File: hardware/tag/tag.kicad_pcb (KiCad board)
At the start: 2 copper layers, 96.5 x 48.3 mm, 14 parts

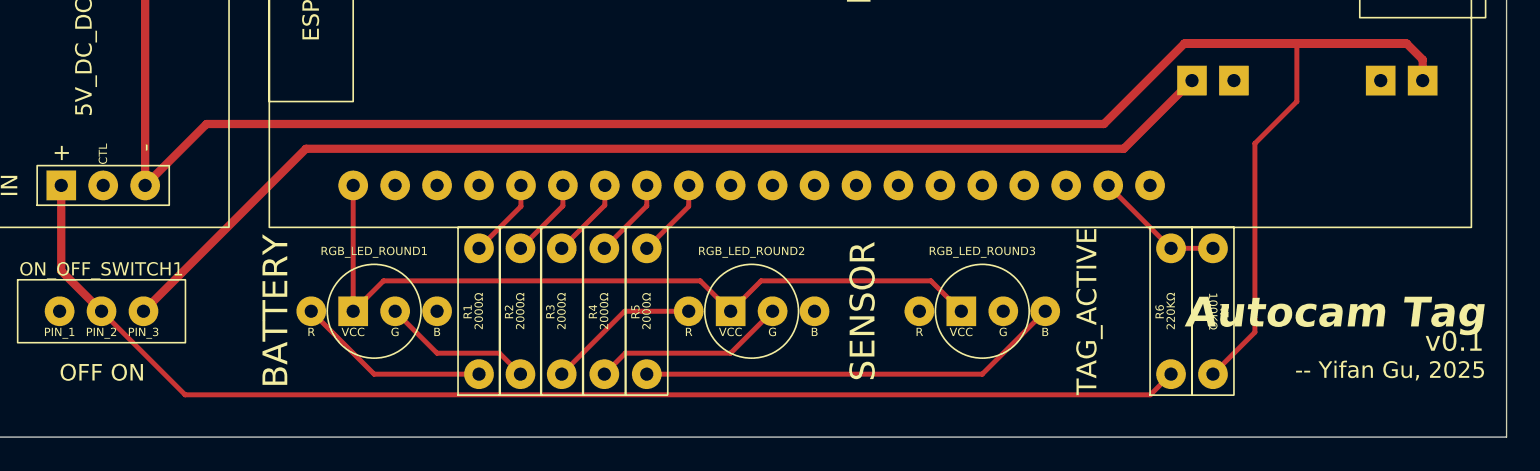
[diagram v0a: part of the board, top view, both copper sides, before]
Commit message: hardware/tag: Remove the tag active led.
The tag has not turned on the BLE yet.
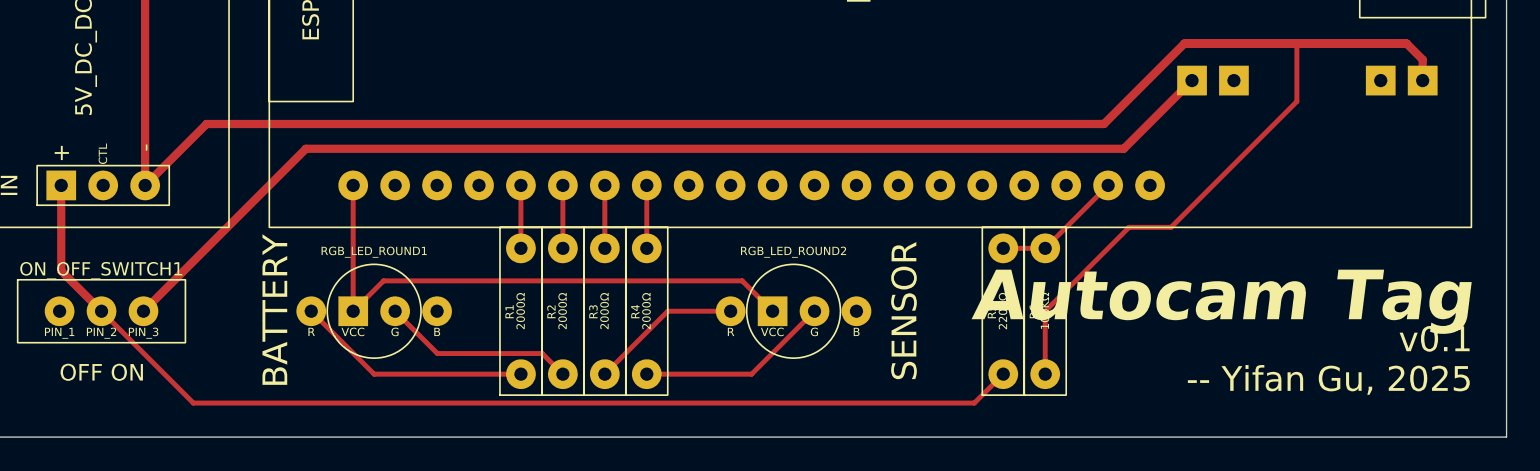
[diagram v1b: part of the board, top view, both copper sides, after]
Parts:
- removed the R5 at (143.5, 120.7)
- removed RGB_LED_ROUND3: TAG_ACTIVE, Autocam:Anode RGB LED (Round)
- moved R6 12.7 mm to (167.6, 120.7), turned to 90 degrees
- moved R5 10.2 mm to (165.1, 120.7)
- moved R3 2.61 mm to (141.0, 120.7)
- moved R2 2.57 mm to (138.4, 120.7)
- moved R4 2.57 mm to (143.5, 120.7)
- moved R1 2.54 mm to (135.9, 120.7)
- moved RGB_LED_ROUND2 2.54 mm to (152.4, 116.8)
- renumbered R6 to R5, R7 to R6
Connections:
- ESP32_UWB1 pad 9: Net-(ESP32_UWB1-IO15) -> unconnected-(ESP32_UWB1-IO15-Pad9)
- R6 pad 1: Net-(ESP32_UWB1-IO36) -> Net-(Battery_Charger1-OUT-)
- R6 pad 2: Net-(Battery_Charger1-OUT-) -> Net-(ESP32_UWB1-IO36)
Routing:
- net Net-(RGB_LED_ROUND3-B): track 25.7 -> 0.00 mm
- net Net-(ESP32_UWB1-3V3): track 47.5 -> 34.5 mm
- net Net-(5V_DC_DC_Converter1-+-Pad1): track 76.0 -> 66.3 mm
- net Net-(Battery_Charger1-OUT-): track 161.9 -> 167.6 mm
- net Net-(ESP32_UWB1-IO15): track 4.90 -> 0.00 mm
- net Net-(RGB_LED_ROUND1-G): track 9.17 -> 11.7 mm
- net Net-(RGB_LED_ROUND1-R): track 11.7 -> 14.3 mm
- net Net-(ESP32_UWB1-IO14): track 5.48 -> 4.32 mm
- net Net-(ESP32_UWB1-IO13): track 4.93 -> 3.85 mm
- net Net-(ESP32_UWB1-IO12): track 4.87 -> 3.81 mm
- net Net-(ESP32_UWB1-IO2): track 4.86 -> 3.81 mm

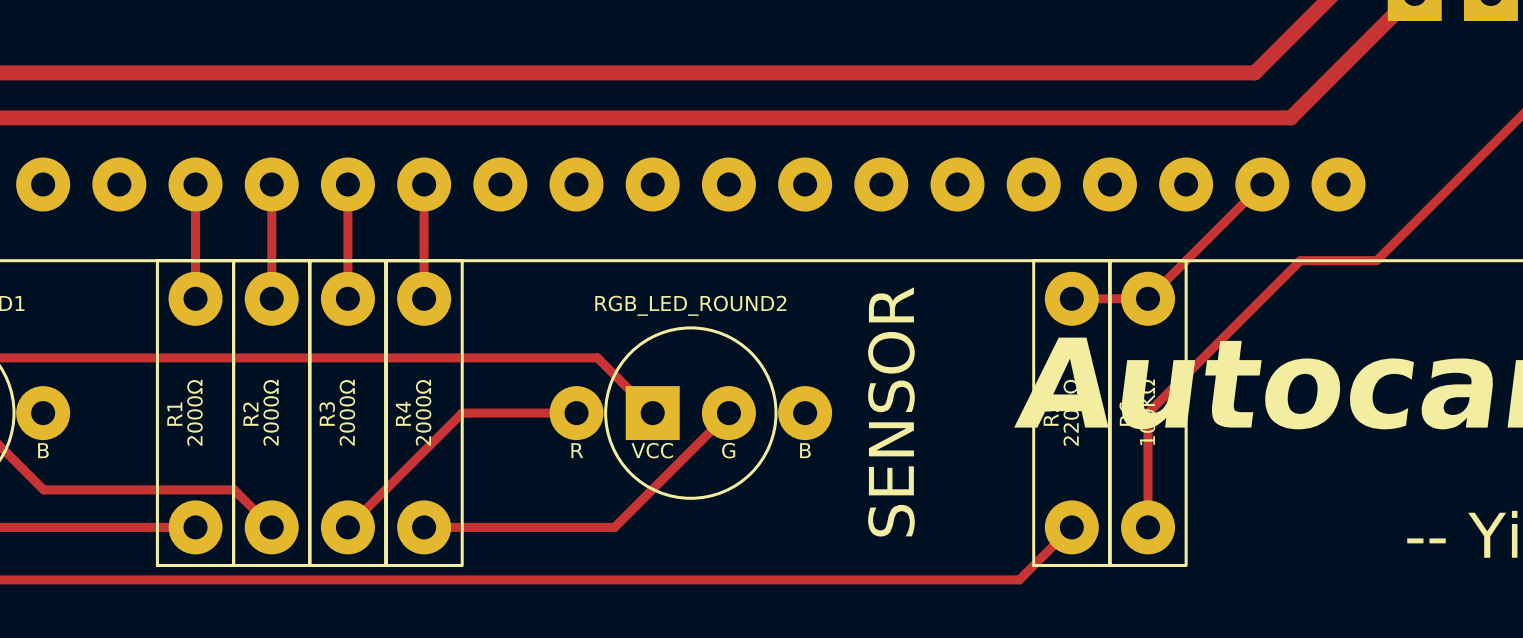
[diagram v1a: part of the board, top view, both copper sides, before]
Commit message: hardware: Increase the LED resistor from 2000Ω to 10KΩ.
To reduce the power consumption.
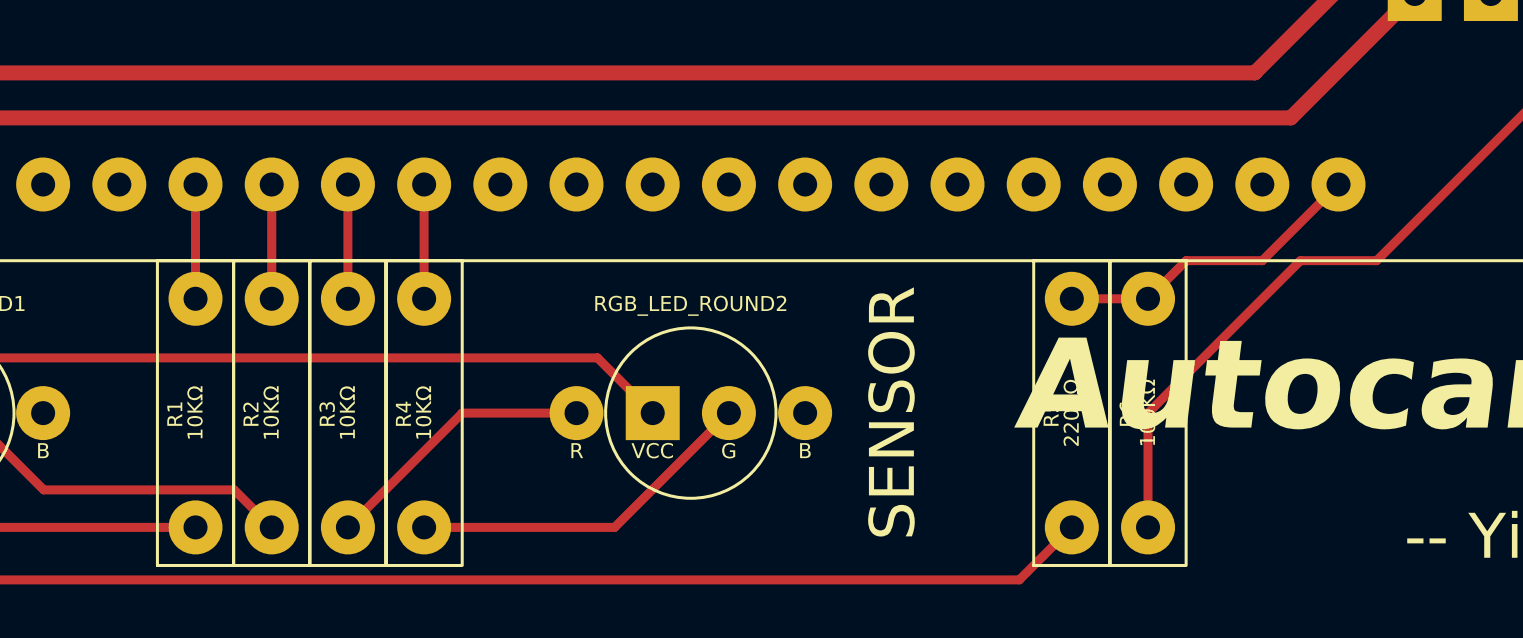
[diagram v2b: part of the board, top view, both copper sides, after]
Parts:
- R1, R2, R3, R4: value 2000Ω -> 10KΩ
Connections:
- ESP32_UWB1 pad 19: Net-(ESP32_UWB1-IO36) -> unconnected-(ESP32_UWB1-IO36-Pad19)
- ESP32_UWB1 pad 20: unconnected-(ESP32_UWB1-IO39-Pad20) -> Net-(ESP32_UWB1-IO39)
- R5 pad 2: Net-(ESP32_UWB1-IO36) -> Net-(ESP32_UWB1-IO39)
- R6 pad 2: Net-(ESP32_UWB1-IO36) -> Net-(ESP32_UWB1-IO39)
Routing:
- net Net-(ESP32_UWB1-IO39): track 0.00 -> 10.5 mm
- net Net-(ESP32_UWB1-IO36): track 7.93 -> 0.00 mm
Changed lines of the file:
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@@
 	(net 7 "Net-(ESP32_UWB1-IO2)")
 	(net 8 "Net-(ESP32_UWB1-3V3)")
-	(net 9 "Net-(ESP32_UWB1-IO36)")
+	(net 9 "Net-(ESP32_UWB1-IO39)")
 	(net 10 "unconnected-(ESP32_UWB1-IO21-Pad30)")
 	(net 11 "unconnected-(ESP32_UWB1-IO35-Pad18)")
@@
 	(net 26 "unconnected-(ESP32_UWB1-RST-Pad3)")
 	(net 27 "unconnected-(ESP32_UWB1-IO18-Pad10)")
-	(net 28 "unconnected-(ESP32_UWB1-IO39-Pad20)")
+	(net 28 "unconnected-(ESP32_UWB1-IO36-Pad19)")
 	(net 29 "unconnected-(ESP32_UWB1-IO23-Pad32)")
 	(net 30 "unconnected-(ESP32_UWB1-GND-Pad2)")
@@
 			(layers "*.Cu" "*.Mask")
 			(remove_unused_layers no)
-			(net 9 "Net-(ESP32_UWB1-IO36)")
+			(net 28 "unconnected-(ESP32_UWB1-IO36-Pad19)")
 			(pinfunction "IO36")
 			(pintype "bidirectional")
@@
 			(layers "*.Cu" "*.Mask")
 			(remove_unused_layers no)
-			(net 28 "unconnected-(ESP32_UWB1-IO39-Pad20)")
+			(net 9 "Net-(ESP32_UWB1-IO39)")
 			(pinfunction "IO39")
 			(pintype "bidirectional")
@@
 			)
 		)
-		(property "Value" "2000Ω"
+		(property "Value" "10KΩ"
 			(at 3.81 0 90)
 			(unlocked yes)
@@
 			)
 		)
-		(property "Value" "2000Ω"
+		(property "Value" "10KΩ"
 			(at 3.81 0 90)
 			(unlocked yes)
@@
 			)
 		)
-		(property "Value" "2000Ω"
+		(property "Value" "10KΩ"
 			(at 3.81 0 90)
 			(unlocked yes)
@@
 			)
 		)
-		(property "Value" "2000Ω"
+		(property "Value" "10KΩ"
 			(at 3.81 0 90)
 			(unlocked yes)
@@
 			(layers "*.Cu" "*.Mask")
 			(remove_unused_layers no)
-			(net 9 "Net-(ESP32_UWB1-IO36)")
+			(net 9 "Net-(ESP32_UWB1-IO39)")
 			(pintype "passive")
 		)
@@
 			(layers "*.Cu" "*.Mask")
 			(remove_unused_layers no)
-			(net 9 "Net-(ESP32_UWB1-IO36)")
+			(net 9 "Net-(ESP32_UWB1-IO39)")
 			(pintype "passive")
 		)
@@
 	)
 	(segment
-		(start 171.45 109.22)
-		(end 167.64 113.03)
+		(start 171.45 111.76)
+		(end 173.99 109.22)
+		(width 0.3)
+		(layer "F.Cu")
+		(net 9)
+	)
+	(segment
+		(start 167.64 113.03)
+		(end 168.91 111.76)
 		(width 0.3)
 		(layer "F.Cu")
@@
 		(width 0.3)
 		(layer "F.Cu")
+		(net 9)
+	)
+	(segment
+		(start 168.91 111.76)
+		(end 171.45 111.76)
+		(width 0.3)
+		(layer "F.Cu")

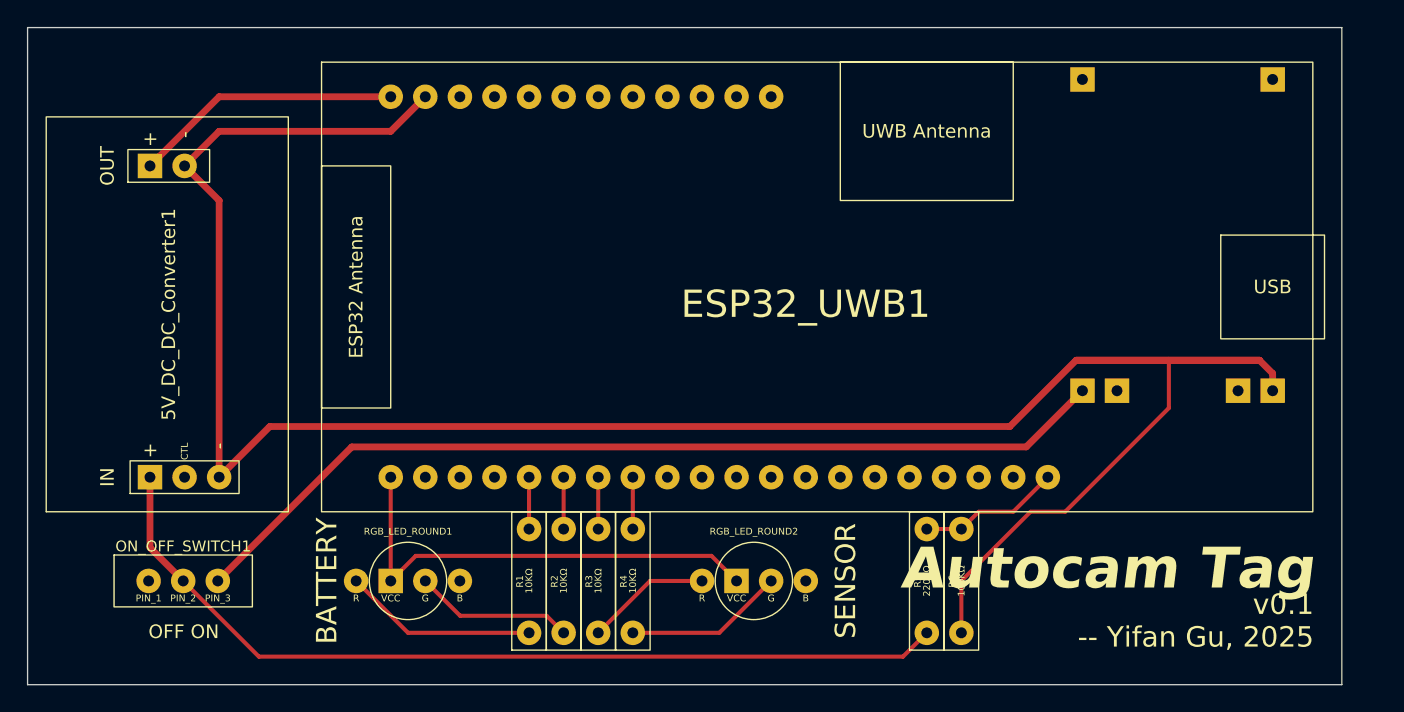
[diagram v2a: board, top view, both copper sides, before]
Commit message: hardware: Reroute the wires to fix unavailable PINs.
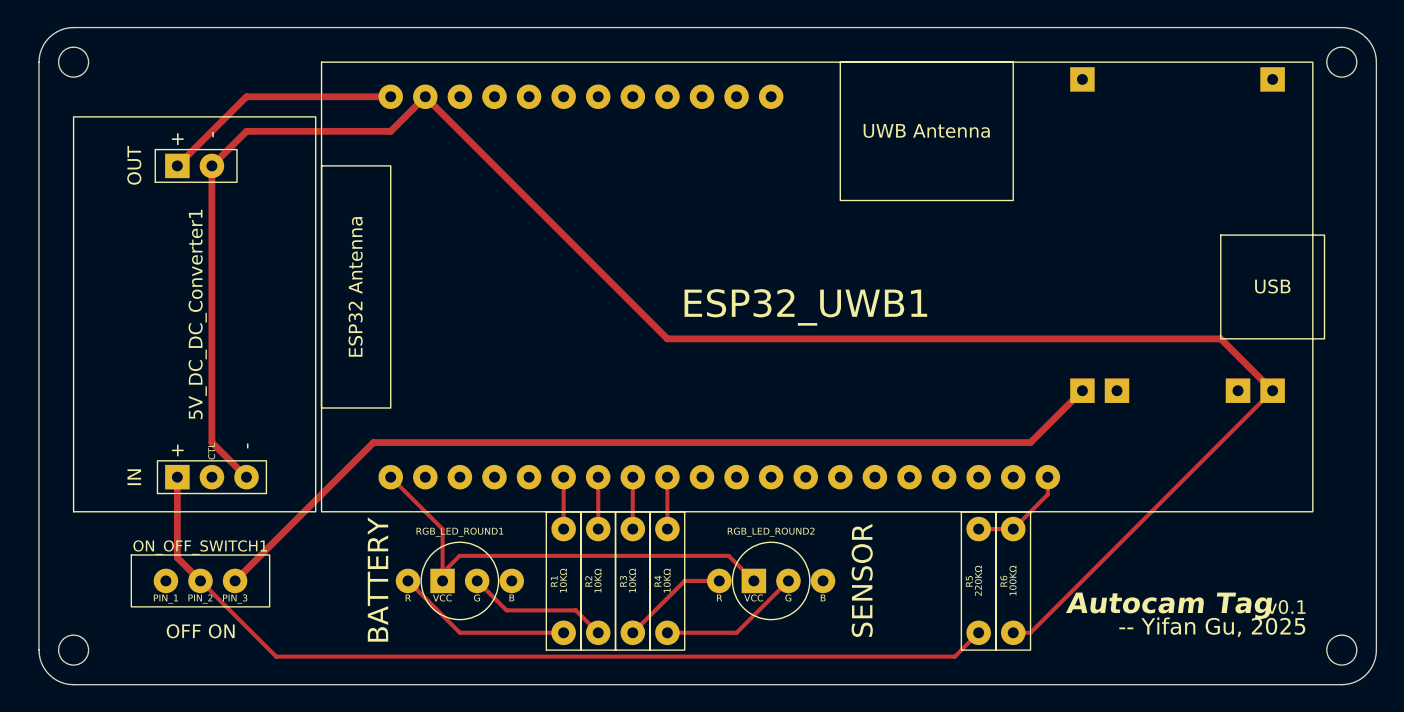
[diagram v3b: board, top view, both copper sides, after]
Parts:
- added REF**: MountingHole_2.2mm_M2, MountingHole:MountingHole_2.2mm_M2, F.Cu at (195.6, 121.9)
- added REF**: MountingHole_2.2mm_M2, MountingHole:MountingHole_2.2mm_M2, F.Cu at (195.6, 78.7)
- added REF**: MountingHole_2.2mm_M2, MountingHole:MountingHole_2.2mm_M2, F.Cu at (102.4, 78.7)
- added REF**: MountingHole_2.2mm_M2, MountingHole:MountingHole_2.2mm_M2, F.Cu at (102.4, 121.9)
- moved R5 3.81 mm to (168.9, 120.7)
- moved R6 3.81 mm to (171.4, 120.7)
- moved RGB_LED_ROUND1 3.81 mm to (130.8, 116.8)
- moved R1 2.54 mm to (138.4, 120.7)
- moved R4 2.54 mm to (146.1, 120.7)
- moved R2 2.54 mm to (141.0, 120.7)
- moved R3 2.54 mm to (143.5, 120.7)
- moved 5V_DC_DC_Converter1 2.01 mm to (102.4, 111.8)
- moved ON_OFF_SWITCH1 1.27 mm to (109.2, 116.8)
- moved RGB_LED_ROUND2 1.27 mm to (153.7, 116.8)
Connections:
- ESP32_UWB1 pad 5: Net-(ESP32_UWB1-IO2) -> unconnected-(ESP32_UWB1-IO2-Pad5)
- ESP32_UWB1 pad 9: unconnected-(ESP32_UWB1-IO15-Pad9) -> Net-(ESP32_UWB1-IO15)
- R1 pad 2: Net-(ESP32_UWB1-IO2) -> Net-(ESP32_UWB1-IO12)
- R2 pad 2: Net-(ESP32_UWB1-IO12) -> Net-(ESP32_UWB1-IO13)
- R3 pad 2: Net-(ESP32_UWB1-IO13) -> Net-(ESP32_UWB1-IO14)
- R4 pad 2: Net-(ESP32_UWB1-IO14) -> Net-(ESP32_UWB1-IO15)
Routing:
- net Net-(Battery_Charger1-OUT-): track 167.6 -> 139.3 mm
- net Net-(ESP32_UWB1-IO2): track 3.81 -> 0.00 mm
- net Net-(ESP32_UWB1-IO15): track 0.00 -> 3.81 mm
- net Net-(ESP32_UWB1-IO39): track 10.5 -> 7.40 mm
- net Net-(5V_DC_DC_Converter1-+-Pad1): track 66.3 -> 68.5 mm
- net Net-(ESP32_UWB1-5V0): track 19.8 -> 17.8 mm
- net Net-(RGB_LED_ROUND2-G): track 11.7 -> 10.5 mm
- net Net-(RGB_LED_ROUND1-G): track 11.7 -> 10.5 mm
- net Net-(Battery_Charger1-OUT+): track 69.3 -> 68.0 mm
- net Net-(RGB_LED_ROUND2-R): track 9.20 -> 7.93 mm
- net Net-(RGB_LED_ROUND1-R): track 14.3 -> 13.0 mm
- net Net-(ESP32_UWB1-3V3): track 34.5 -> 33.9 mm
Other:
- board size 96.5 x 48.3 mm -> 98.2 x 48.3 mm
